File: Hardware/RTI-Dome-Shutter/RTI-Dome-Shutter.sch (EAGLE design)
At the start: 42 parts, among them IC1 24AA128ST, IC5 74LVC245, IC6 74ABT245, J1 POWERPOLE_POWER45A

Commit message: Fix merge conflict
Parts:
- R1, R3: value 2.2K -> 1K
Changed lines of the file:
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@@
 <part name="IC1" library="microchip" deviceset="24*" device="ST" technology="AA128"/>
 <part name="GND8" library="supply1" deviceset="GND" device=""/>
-<part name="R1" library="rti" deviceset="R-EU" device="'0805'" value="2.2K"/>
-<part name="R3" library="rti" deviceset="R-EU" device="'0805'" value="2.2K"/>
+<part name="R1" library="rti" deviceset="R-EU" device="'0805'" value="1K"/>
+<part name="R3" library="rti" deviceset="R-EU" device="'0805'" value="1K"/>
 <part name="C5" library="rti" deviceset="C-EU" device="'0805'" value="100nF"/>
 <part name="GND12" library="supply1" deviceset="GND" device=""/>

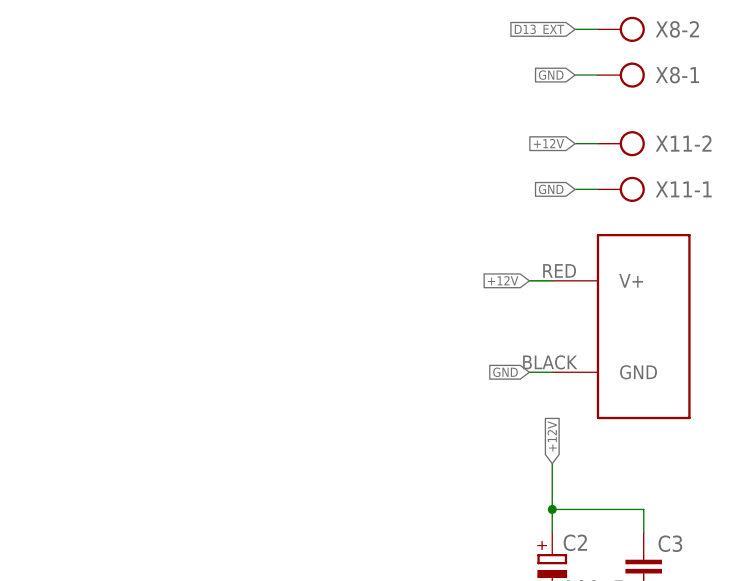
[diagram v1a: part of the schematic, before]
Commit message: Started working on a new version using the Raspberry Pi RP2040 as a future replacement for the Arduino DUE
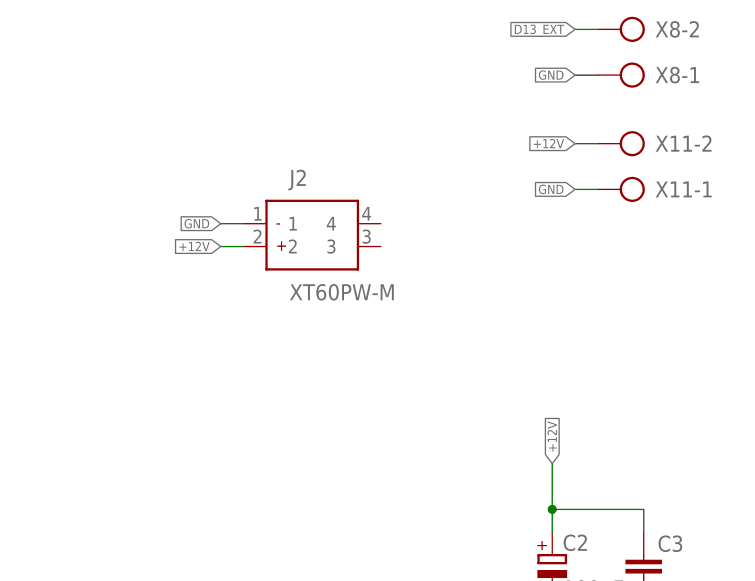
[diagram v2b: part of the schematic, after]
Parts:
- removed J1: POWERPOLE_POWER45A, powerpoles:POWERPOLE_POWER45A
- added J2: XT60PW-M, samacsys:XT60PW-M
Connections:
- net +12V: now also J2.2; no longer J1.V+
- net GND: now also J2.1; no longer J1.GND
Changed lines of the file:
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@@
 <setting verticaltext="up"/>
 </settings>
-<grid distance="0.1" unitdist="inch" unit="inch" style="lines" multiple="1" display="no" altdistance="0.01" altunitdist="inch" altunit="inch"/>
+<grid distance="1.27" unitdist="mm" unit="mm" style="lines" multiple="1" display="no" altdistance="0.127" altunitdist="mm" altunit="mm"/>
 <layers>
 <layer number="1" name="Top" color="4" fill="1" visible="no" active="no"/>
 <layer number="2" name="Route2" color="1" fill="3" visible="no" active="no"/>
 <layer number="3" name="Route3" color="4" fill="3" visible="no" active="no"/>
+<layer number="4" name="Route4" color="18" fill="4" visible="no" active="no"/>
+<layer number="5" name="Route5" color="19" fill="4" visible="no" active="no"/>
+<layer number="6" name="Route6" color="25" fill="8" visible="no" active="no"/>
+<layer number="7" name="Route7" color="26" fill="8" visible="no" active="no"/>
+<layer number="8" name="Route8" color="27" fill="2" visible="no" active="no"/>
+<layer number="9" name="Route9" color="28" fill="2" visible="no" active="no"/>
+<layer number="10" name="Route10" color="29" fill="7" visible="no" active="no"/>
+<layer number="11" name="Route11" color="30" fill="7" visible="no" active="no"/>
+<layer number="12" name="Route12" color="20" fill="5" visible="no" active="no"/>
+<layer number="13" name="Route13" color="21" fill="5" visible="no" active="no"/>
 <layer number="14" name="Route14" color="1" fill="6" visible="no" active="no"/>
 <layer number="15" name="Route15" color="4" fill="6" visible="no" active="no"/>
@@
 <part name="IC6" library="rti" deviceset="74*245" device="" technology="ABT" value="74ABT245"/>
 <part name="GND7" library="supply1" deviceset="GND" device=""/>
-<part name="J1" library="powerpoles" deviceset="POWERPOLE_POWER" device="45A"/>
 <part name="U$1" library="MCP120T" deviceset="MCP120T" device="" value="MCP120T-315I/TT">
 <attribute name="MPN" value="MCP120T-315I/TT"/>
@@
 <part name="GND11" library="supply1" deviceset="GND" device=""/>
 <part name="R11" library="rti" deviceset="R-EU" device="'0805'" value="100"/>
+<part name="J2" library="samacsys" library_urn="urn:adsk.eagle:library:37256869" deviceset="XT60PW-M" device="" package3d_urn="urn:adsk.eagle:package:37256940/5"/>
 </parts>
 <sheets>
@@
 <attribute name="VALUE" x="185.42" y="223.52" size="1.778" layer="96"/>
 </instance>
-<instance part="J1" gate="G$1" x="378.46" y="83.82" smashed="yes"/>
 <instance part="U$1" gate="G$1" x="218.44" y="93.98" smashed="yes">
 <attribute name="MPN" x="218.44" y="93.98" size="1.778" layer="96" display="off"/>
@@
 <attribute name="NAME" x="87.63" y="130.5814" size="1.778" layer="95" rot="R180"/>
 <attribute name="VALUE" x="87.63" y="135.382" size="1.778" layer="96" rot="R180"/>
+</instance>
+<instance part="J2" gate="G$1" x="341.63" y="95.25" smashed="yes">
+<attribute name="NAME" x="339.09" y="100.33" size="1.778" layer="95" align="center-left"/>
+<attribute name="VALUE" x="339.09" y="87.63" size="1.778" layer="96" align="center-left"/>
 </instance>
 </instances>
@@
 <junction x="121.92" y="170.18"/>
 <pinref part="IC5" gate="P" pin="GND"/>
-</segment>
-<segment>
-<wire x1="365.76" y1="78.74" x2="368.3" y2="78.74" width="0.1524" layer="91"/>
-<label x="365.76" y="78.74" size="1.016" layer="95" rot="R180" xref="yes"/>
-<pinref part="J1" gate="G$1" pin="GND"/>
 </segment>
 <segment>
@@
 <label x="116.84" y="236.22" size="1.016" layer="95" rot="R180" xref="yes"/>
 </segment>
+<segment>
+<pinref part="J2" gate="G$1" pin="1"/>
+<wire x1="331.47" y1="95.25" x2="334.01" y2="95.25" width="0.1524" layer="91"/>
+<label x="331.47" y="95.25" size="1.016" layer="95" ratio="4" rot="R180" xref="yes"/>
+</segment>
 </net>
 <net name="+12V" class="1">
@@
 </segment>
 <segment>
-<wire x1="365.76" y1="88.9" x2="368.3" y2="88.9" width="0.1524" layer="91"/>
-<label x="365.76" y="88.9" size="1.016" layer="95" rot="R180" xref="yes"/>
-<pinref part="J1" gate="G$1" pin="V+"/>
-</segment>
-<segment>
 <wire x1="370.84" y1="104.14" x2="373.38" y2="104.14" width="0.1524" layer="91"/>
 <label x="370.84" y="104.14" size="1.016" layer="95" rot="MR0" xref="yes"/>
 <pinref part="X11" gate="-2" pin="KL"/>
+</segment>
+<segment>
+<pinref part="J2" gate="G$1" pin="2"/>
+<wire x1="331.47" y1="92.71" x2="334.01" y2="92.71" width="0.1524" layer="91"/>
+<label x="331.47" y="92.71" size="1.016" layer="95" ratio="4" rot="R180" xref="yes"/>
 </segment>
 </net>
@@
 </schematic>
 </drawing>
+<compatibility>
+<note version="8.2" severity="warning">
+Since Version 8.2, EAGLE supports online libraries. The ids
+of those online libraries will not be understood (or retained)
+with this version.
+</note>
+<note version="8.3" severity="warning">
+Since Version 8.3, EAGLE supports URNs for individual library
+assets (packages, symbols, and devices). The URNs of those assets
+will not be understood (or retained) with this version.
+</note>
+<note version="8.3" severity="warning">
+Since Version 8.3, EAGLE supports the association of 3D packages
+with devices in libraries, schematics, and board files. Those 3D
+packages will not be understood (or retained) with this version.
+</note>
+</compatibility>
 </eagle>
